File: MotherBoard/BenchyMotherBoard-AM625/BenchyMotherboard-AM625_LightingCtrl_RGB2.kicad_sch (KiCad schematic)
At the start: 10 parts, among them J22 B4B-XH-AM, Q13 PMXB43UNEZ, Q14 PMXB43UNEZ, Q15 PMXB43UNEZ

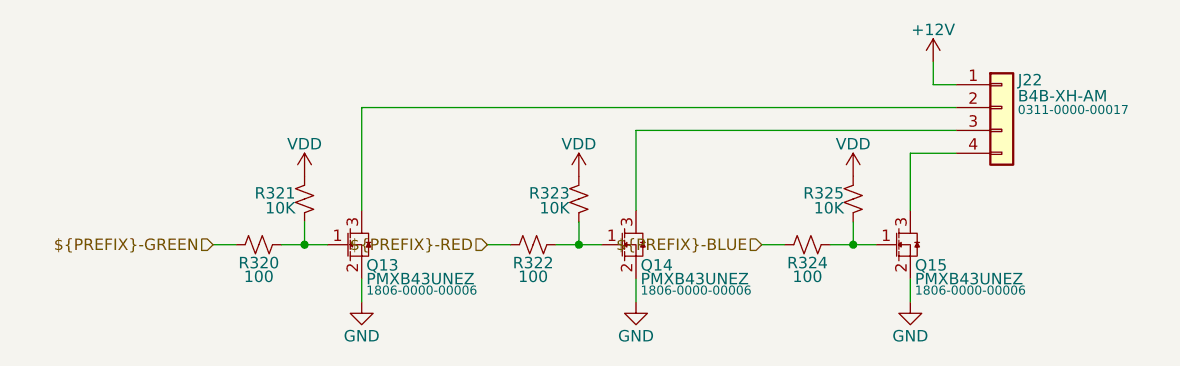
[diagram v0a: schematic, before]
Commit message: Schematic capture mostly complete. Starting PCB layout
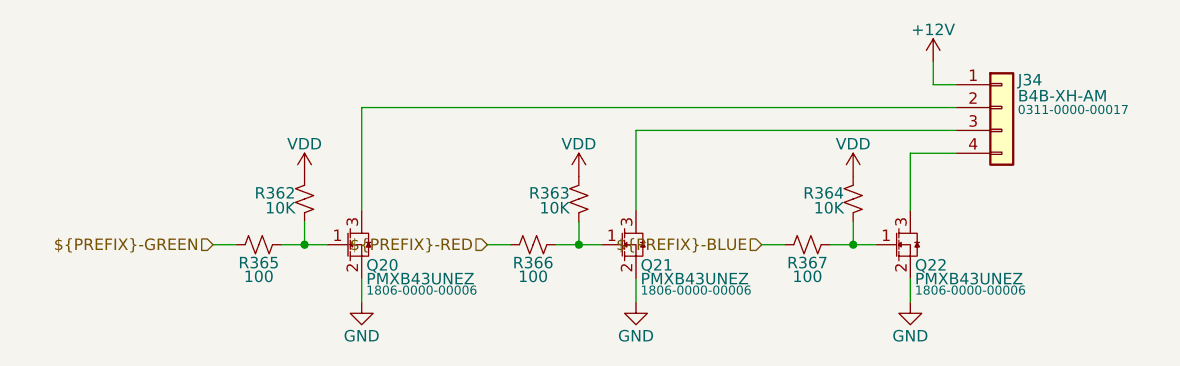
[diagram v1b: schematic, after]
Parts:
- removed J22: B4B-XH-AM, Connector_JST:JST_XH_B4B-XH-A_1x04_P2.50mm_Vertical, symbol DX_Connector_JST:B4B-XH-A
- removed Q13, Q14, Q15: PMXB43UNEZ, Daxxn_Packages:DFN1010D-3, symbol DX_Transistor_MOSFET:PMXB43UNEZ
- removed R320, R322, R324: 100, Daxxn_Standard_Resistors:RES_0402, symbol DX_Resistor:RC0402JR-07100RL
- removed R321, R323, R325: 10K, Daxxn_Standard_Resistors:RES_0402, symbol DX_Resistor:RC0402JR-0710KL
- added J34: B4B-XH-AM, Connector_JST:JST_XH_B4B-XH-A_1x04_P2.50mm_Vertical, symbol DX_Connector_JST:B4B-XH-A
- added Q20, Q21, Q22: PMXB43UNEZ, Daxxn_Packages:DFN1010D-3, symbol DX_Transistor_MOSFET:PMXB43UNEZ
- added R362, R363, R364: 10K, Daxxn_Standard_Resistors:RES_0402, symbol DX_Resistor:RC0402JR-0710KL
- added R365, R366, R367: 100, Daxxn_Standard_Resistors:RES_0402, symbol DX_Resistor:RC0402JR-07100RL
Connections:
- net ${PREFIX}-BLUE: now also R367.1
- net ${PREFIX}-GREEN: now also R365.1
- net ${PREFIX}-RED: now also R366.1
- net +12V: now also J34.1 (Pin_1)
- net GND: now also Q20.2 (S), Q21.2 (S), Q22.2 (S)
- net VDD: now also R362.1, R363.1, R364.1
- new net: Q22.1 (G), R364.2, R367.2
- new net: Q21.1 (G), R363.2, R366.2
- new net: Q20.1 (G), R362.2, R365.2
- new net: J34.4 (Pin_4), Q22.3 (D)
- new net: J34.2 (Pin_2), Q20.3 (D)
- new net: J34.3 (Pin_3), Q21.3 (D)
